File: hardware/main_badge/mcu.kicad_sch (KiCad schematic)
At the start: 19 parts, among them U1 RP2350B, U2 W25Q128JVS, Y1 12MHz

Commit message: main board done except for placing LEDs and drawing ears... I think
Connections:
- net CAM_XCLK: no longer names the net of U1.19 (GPIO19)
- no-connect marks 0 -> 1
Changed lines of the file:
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@@
 		(color 0 0 0 0)
 	)
+	(no_connect
+		(at 207.01 106.68)
+	)
 	(wire
 		(pts
@@
 			(effects
 				(font
-					(size 1.27 1.27)
-				)
-				(justify left)
-				(hide yes)
-			)
-		)
-	)
-	(global_label "CAM_XCLK"
-		(shape input)
-		(at 207.01 106.68 0)
-		(fields_autoplaced yes)
-		(effects
-			(font
-				(size 1.27 1.27)
-			)
-			(justify left)
-		)
-		(property "Intersheetrefs" "${INTERSHEET_REFS}"
-			(at 219.5504 106.68 0)
-			(effects
-				(font

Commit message: screen LEDs placed, photo button removed
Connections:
- net PHOTO: no longer names the net of U1.53 (GPIO42/ADC2)
- no-connect marks 1 -> 2
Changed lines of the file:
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@@
+	)
+	(no_connect
+		(at 119.38 144.78)
 	)
 	(no_connect
@@
 	(wire
 		(pts
-			(xy 111.76 144.78) (xy 119.38 144.78)
-		)
-		(stroke
-			(width 0)
-			(type default)
-		)
-	)
-	(wire
-		(pts
 			(xy 63.5 35.56) (xy 71.12 35.56)
 		)
@@
 				(hide yes)
 			)
-		)
-	)
-	(global_label "PHOTO"
-		(shape input)
-		(at 111.76 144.78 180)
-		(fields_autoplaced yes)
-		(effects
-			(font
-				(size 1.27 1.27)
-			)
-			(justify right)
-		)
-		(property "Intersheetrefs" "${INTERSHEET_REFS}"
-			(at 102.5457 144.78 0)
-			(effects
-				(font
-					(size 1.27 1.27)
-				)
-				(justify right)
-				(hide yes)
-			)

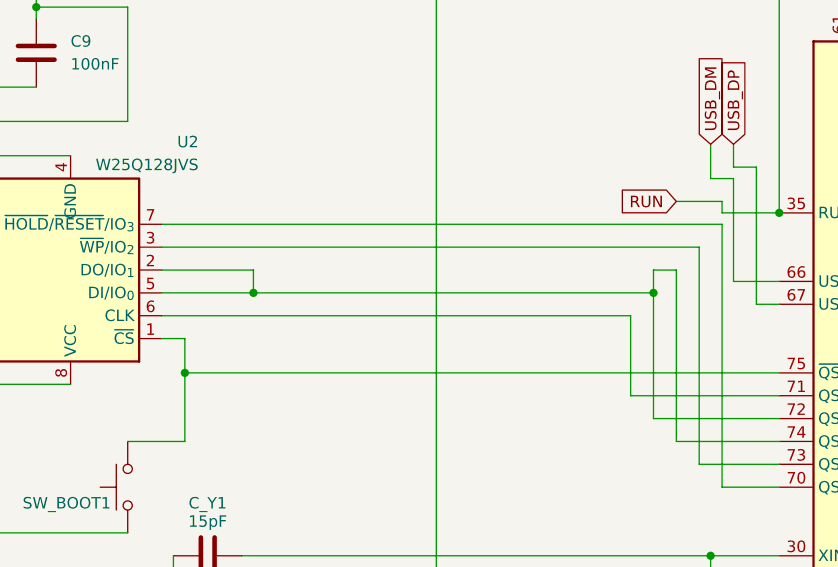
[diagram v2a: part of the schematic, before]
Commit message: USB port and chip routed
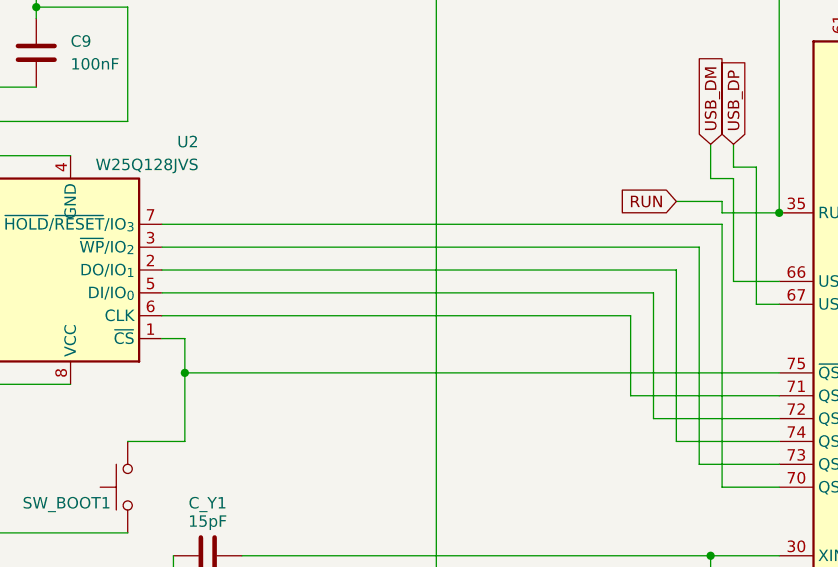
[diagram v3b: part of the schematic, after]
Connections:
- net at U1.72 (QSPI_SD0), U2.5 (DI/IO_{0}): no longer U1.74 (QSPI_SD1), U2.2 (DO/IO_{1})
- new net: U1.74 (QSPI_SD1), U2.2 (DO/IO_{1})
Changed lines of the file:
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@@
-	)
-	(junction
-		(at 105.41 82.55)
-		(diameter 0)
-		(color 0 0 0 0)
 	)
 	(junction
@@
 		(color 0 0 0 0)
 	)
-	(junction
-		(at 60.96 82.55)
-		(diameter 0)
-		(color 0 0 0 0)
-	)
 	(no_connect
 		(at 119.38 144.78)
@@
 	(wire
 		(pts
-			(xy 105.41 80.01) (xy 105.41 82.55)
-		)
-		(stroke
-			(width 0)
-			(type default)
-		)
-	)
-	(wire
-		(pts
 			(xy 97.79 22.86) (xy 97.79 25.4)
 		)
@@
 	(wire
 		(pts
-			(xy 50.8 82.55) (xy 60.96 82.55)
+			(xy 50.8 82.55) (xy 105.41 82.55)
 		)
 		(stroke
@@
 	(wire
 		(pts
-			(xy 60.96 80.01) (xy 50.8 80.01)
+			(xy 50.8 80.01) (xy 107.95 80.01)
 		)
 		(stroke
@@
 	(wire
 		(pts
-			(xy 105.41 80.01) (xy 107.95 80.01)
-		)
-		(stroke
-			(width 0)
-			(type default)
-		)
-	)
-	(wire
-		(pts
 			(xy 144.78 170.18) (xy 172.72 170.18)
 		)
@@
 	(wire
 		(pts
-			(xy 60.96 82.55) (xy 105.41 82.55)
-		)
-		(stroke
-			(width 0)
-			(type default)
-		)
-	)
-	(wire
-		(pts
 			(xy 119.38 121.92) (xy 111.76 121.92)
 		)
@@
 		)
 		(stroke
-			(width 0)
-			(type default)
-		)
-	)
-	(wire
-		(pts
-			(xy 60.96 82.55) (xy 60.96 80.01)
-		)
-		(stroke

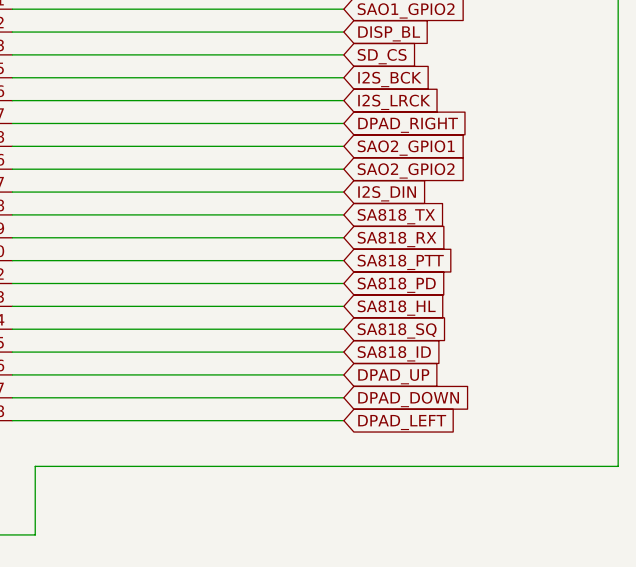
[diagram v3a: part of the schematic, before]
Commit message: traces all fubar, might delete them all and start over.
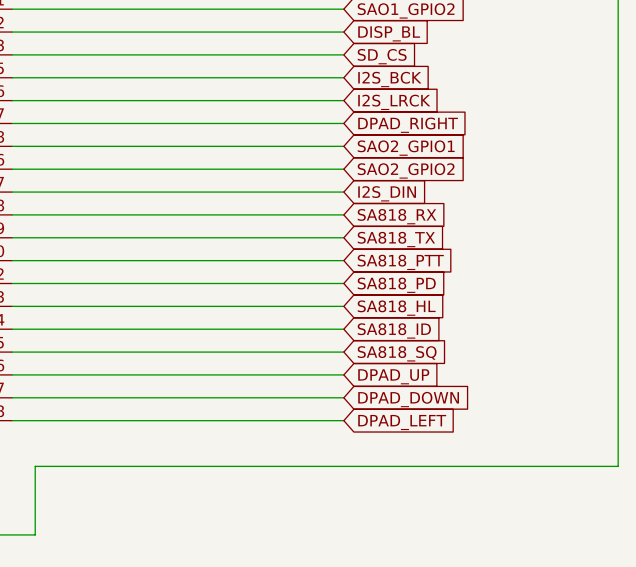
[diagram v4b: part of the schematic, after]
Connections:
- net SA818_ID: now also U1.44 (GPIO35); no longer U1.45 (GPIO36)
- net SA818_RX: now also U1.38 (GPIO30); no longer U1.39 (GPIO31)
- net SA818_SQ: now also U1.45 (GPIO36); no longer U1.44 (GPIO35)
- net SA818_TX: now also U1.39 (GPIO31); no longer U1.38 (GPIO30)

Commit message: updated MCU pin layout
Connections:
- net +3V3: now also R2.2; no longer R2.1
- net AIRPLANE: now also U1.27 (GPIO26); no longer U1.54 (GPIO43/ADC3)
- net DISP_BL: now also U1.37 (GPIO29); no longer U1.22 (GPIO22)
- net DISP_DC: now also U1.19 (GPIO19); no longer U1.3 (GPIO6)
- net DISP_RST: now also U1.54 (GPIO43/ADC3); no longer U1.4 (GPIO7)
- net DPAD_CENTER: now also U1.26 (GPIO25); no longer U1.52 (GPIO41/ADC1)
- net DPAD_DOWN: now also U1.22 (GPIO22); no longer U1.47 (GPIO38)
- net DPAD_LEFT: now also U1.23 (GPIO23); no longer U1.48 (GPIO39)
- net DPAD_RIGHT: now also U1.25 (GPIO24); no longer U1.27 (GPIO26)
- net DPAD_UP: now also U1.21 (GPIO21); no longer U1.46 (GPIO37)
- net I2C_SCL: now also R2.1, U1.56 (GPIO45/ADC5); no longer R2.2, U1.78 (GPIO1)
- net I2C_SDA: now also U1.55 (GPIO44/ADC4); no longer U1.77 (GPIO0)
- net I2S_BCK: now also U1.80 (GPIO3); no longer U1.25 (GPIO24)
- net I2S_DIN: now also U1.79 (GPIO2); no longer U1.37 (GPIO29)
- net I2S_LRCK: now also U1.78 (GPIO1); no longer U1.26 (GPIO25)
- net LED_DATA: now also U1.77 (GPIO0); no longer U1.58 (GPIO47/ADC7)
- net PWR_B: now also U1.40 (GPIO32); no longer U1.57 (GPIO46/ADC6)
- net PWR_G: now also U1.39 (GPIO31); no longer U1.56 (GPIO45/ADC5)
- net PWR_R: now also U1.38 (GPIO30); no longer U1.55 (GPIO44/ADC4)
- net SA818_HL: now also U1.44 (GPIO35); no longer U1.43 (GPIO34)
- net SA818_ID: now also U1.48 (GPIO39); no longer U1.44 (GPIO35)
- net SA818_PD: now also U1.43 (GPIO34); no longer U1.42 (GPIO33)
- net SA818_PTT: now also U1.42 (GPIO33); no longer U1.40 (GPIO32)
- net SA818_RX: now also U1.46 (GPIO37); no longer U1.38 (GPIO30)
- net SA818_SQ: now also U1.47 (GPIO38); no longer U1.45 (GPIO36)
- net SA818_TX: now also U1.45 (GPIO36); no longer U1.39 (GPIO31)
- net SAO1_GPIO1: now also U1.28 (GPIO27); no longer U1.20 (GPIO20)
- net SAO1_GPIO2: now also U1.36 (GPIO28); no longer U1.21 (GPIO21)
- net SAO2_GPIO1: now also U1.52 (GPIO41/ADC1); no longer U1.28 (GPIO27)
- net SAO2_GPIO2: now also U1.53 (GPIO42/ADC2); no longer U1.36 (GPIO28)
- net SD_CS: now also U1.57 (GPIO46/ADC6); no longer U1.23 (GPIO23)
- net SPI_MOSI: now also U1.4 (GPIO7); no longer U1.80 (GPIO3)
- net SPI_SCK: now also U1.3 (GPIO6); no longer U1.79 (GPIO2)
- no-connect marks 2 -> 3
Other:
- moved on the sheet: R1, R2

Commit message: wip routing
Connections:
- net AIRPLANE: now also U1.54 (GPIO43/ADC3); no longer U1.27 (GPIO26)
- net DISP_RST: now also U1.20 (GPIO20); no longer U1.54 (GPIO43/ADC3)
- net SD_CS: now also U1.27 (GPIO26); no longer U1.57 (GPIO46/ADC6)
- no-connect marks 3 -> 2
